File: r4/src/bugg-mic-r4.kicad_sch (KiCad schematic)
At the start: 25 parts, among them J101 2842142-4, U101 PCMD3180

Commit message: Update Wurth spacers to remove DRC violations. DRC pass
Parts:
- H301: renamed from H101; footprint Mounting_Wuerth:Mounting_Wuerth_WA-SMSI-M3_H7mm_9774070360 -> jeffmakes-footprints:Mounting_Wuerth_WA-SMSI-M3_H7mm_9774070360
- H302: renamed from H102; footprint Mounting_Wuerth:Mounting_Wuerth_WA-SMSI-M3_H7mm_9774070360 -> jeffmakes-footprints:Mounting_Wuerth_WA-SMSI-M3_H7mm_9774070360
- renumbered C101 to C301, C102 to C302, C103 to C303, C104 to C304, C105 to C305, C106 to C306, C107 to C307, C108 to C308, C109 to C309, C110 to C310, C111 to C311, C112 to C312, FID1 to FID301, FID2 to FID302, J101 to J301, MIC101 to MIC301, R101 to R301, R102 to R302, R103 to R303, TP102 to TP301, TP103 to TP302, TP101 to TP303, U101 to U301

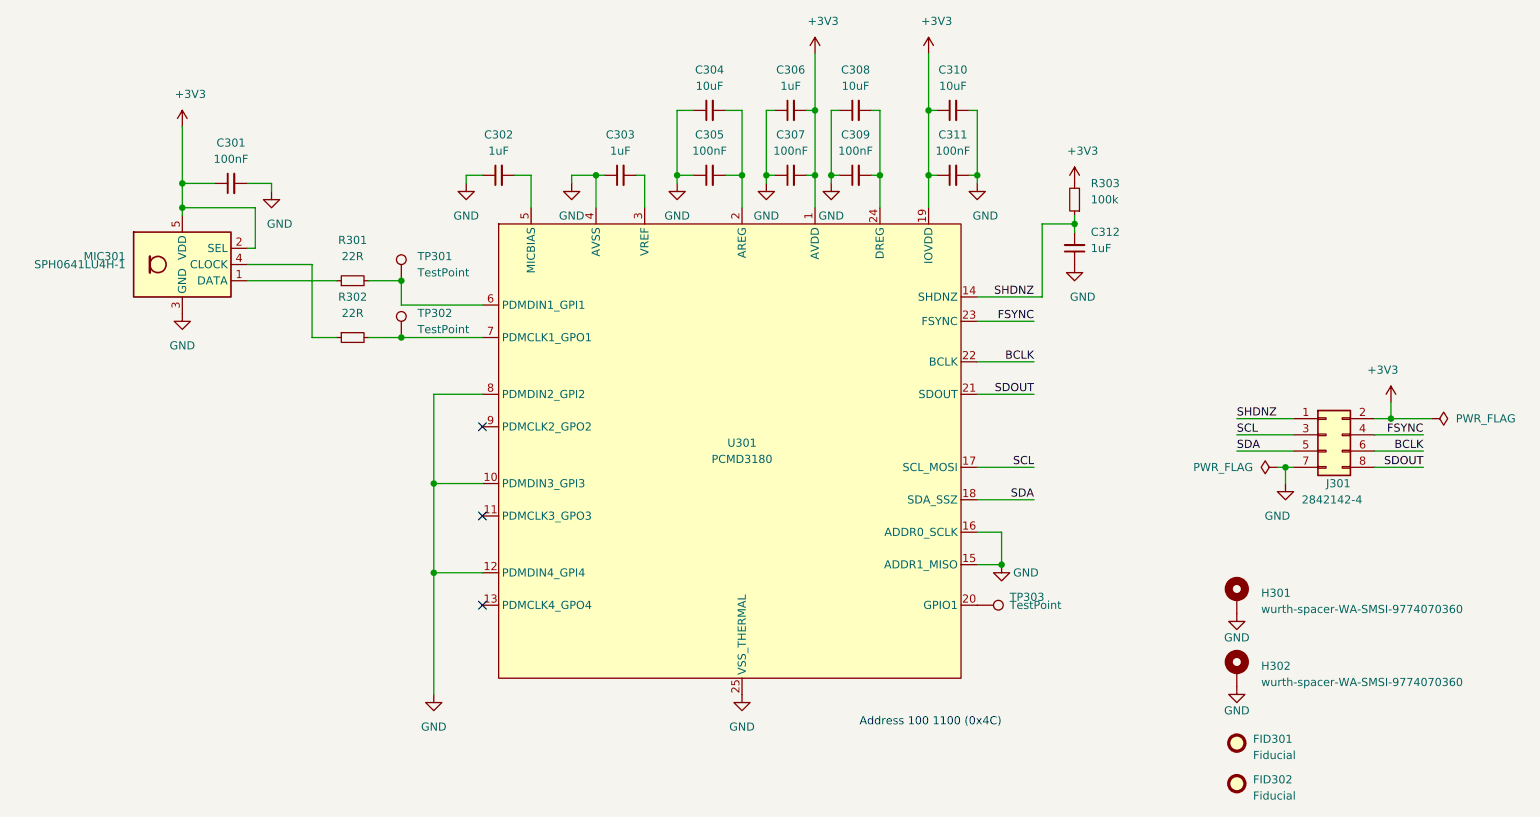
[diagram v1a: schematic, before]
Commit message: Add some cap voltages and other bom-related parameters
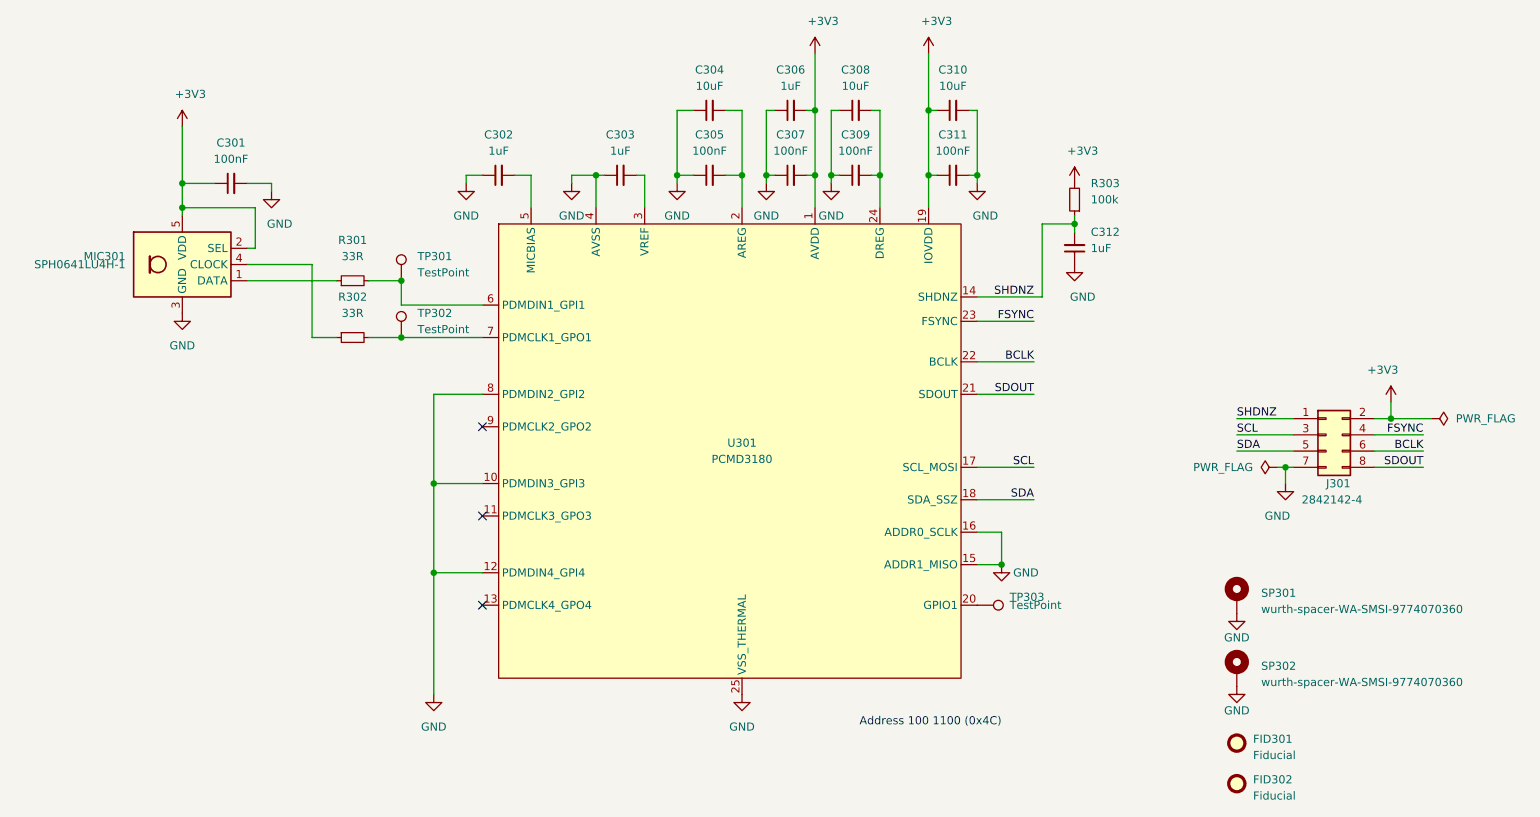
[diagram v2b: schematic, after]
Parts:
- C302, C303, C304, C306, C308, C310: Voltage (none) -> 6.3V
- C312: footprint Capacitor_SMD:C_0603_1608Metric -> Capacitor_SMD:C_0402_1005Metric; Voltage (none) -> 6.3V
- FID301, FID302, TP301, TP302, TP303: now left out of the parts list
- R301, R302: value 22R -> 33R
- renumbered H301 to SP301, H302 to SP302
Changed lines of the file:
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@@
       (effects (font (size 1.27 1.27)))
     )
-    (property "Value" "22R" (at 82.55 80.01 90)
+    (property "Value" "33R" (at 82.55 80.01 90)
       (effects (font (size 1.27 1.27)))
     )
@@
       (project "bugg-mic-r4"
         (path "/1692e6a7-b9c0-4a4a-aa1e-ad946df48101"
-          (reference "R302") (unit 1) (value "22R") (footprint "Resistor_SMD:R_0402_1005Metric")
+          (reference "R302") (unit 1) (value "33R") (footprint "Resistor_SMD:R_0402_1005Metric")
         )
       )
@@
       (effects (font (size 1.27 1.27)) hide)
     )
+    (property "Voltage" "6.3V" (at 105.41 58.42 90)
+      (effects (font (size 1.27 1.27)) hide)
+    )
     (pin "1")
     (pin "2")
@@
   )
   (symbol (lib_id "Connector:TestPoint") (at 90.17 83.82 0) (unit 1)
-    (in_bom yes) (on_board yes) (dnp no)
+    (in_bom no) (on_board yes) (dnp no)
     (property "Reference" "TP302" (at 92.71 80.01 0)
       (effects (font (size 1.27 1.27)) (justify left))
@@
   )
   (symbol (lib_id "Connector:TestPoint") (at 90.17 74.93 0) (unit 1)
-    (in_bom yes) (on_board yes) (dnp no)
+    (in_bom no) (on_board yes) (dnp no)
     (property "Reference" "TP301" (at 92.71 71.12 0)
       (effects (font (size 1.27 1.27)) (justify left))
@@
   (symbol (lib_id "Mechanical:MountingHole_Pad") (at 220.98 135.89 0) (unit 1)
     (in_bom yes) (on_board yes) (dnp no)
-    (property "Reference" "H302" (at 224.79 135.2549 0)
+    (property "Reference" "SP302" (at 224.79 135.2549 0)
       (effects (font (size 1.27 1.27)) (justify left))
     )
@@
       (project "bugg-mic-r4"
         (path "/1692e6a7-b9c0-4a4a-aa1e-ad946df48101"
-          (reference "H302") (unit 1) (value "wurth-spacer-WA-SMSI-9774070360") (footprint "jeffmakes-footprints:Mounting_Wuerth_WA-SMSI-M3_H7mm_9774070360")
+          (reference "SP302") (unit 1) (value "wurth-spacer-WA-SMSI-9774070360") (footprint "jeffmakes-footprints:Mounting_Wuerth_WA-SMSI-M3_H7mm_9774070360")
         )
       )
@@
   )
   (symbol (lib_id "Connector:TestPoint") (at 180.34 125.73 270) (unit 1)
-    (in_bom yes) (on_board yes) (dnp no)
+    (in_bom no) (on_board yes) (dnp no)
     (property "Reference" "TP303" (at 185.42 124.46 90)
       (effects (font (size 1.27 1.27)) (justify left))
@@
       (effects (font (size 1.27 1.27)) hide)
     )
+    (property "Voltage" "6.3V" (at 161.29 48.26 90)
+      (effects (font (size 1.27 1.27)) hide)
+    )
     (pin "1")
     (pin "2")
@@
       (effects (font (size 1.27 1.27)))
     )
-    (property "Value" "22R" (at 82.55 71.12 90)
+    (property "Value" "33R" (at 82.55 71.12 90)
       (effects (font (size 1.27 1.27)))
     )
@@
       (project "bugg-mic-r4"
         (path "/1692e6a7-b9c0-4a4a-aa1e-ad946df48101"
-          (reference "R301") (unit 1) (value "22R") (footprint "Resistor_SMD:R_0402_1005Metric")
+          (reference "R301") (unit 1) (value "33R") (footprint "Resistor_SMD:R_0402_1005Metric")
         )
       )
@@
   )
   (symbol (lib_id "Mechanical:Fiducial") (at 220.98 147.32 0) (unit 1)
-    (in_bom yes) (on_board yes) (dnp no) (fields_autoplaced)
+    (in_bom no) (on_board yes) (dnp no) (fields_autoplaced)
     (property "Reference" "FID301" (at 223.52 146.6849 0)
       (effects (font (size 1.27 1.27)) (justify left))
@@
       (effects (font (size 1.27 1.27)) (justify right))
     )
-    (property "Footprint" "Capacitor_SMD:C_0603_1608Metric" (at 195.58 69.85 0)
+    (property "Footprint" "Capacitor_SMD:C_0402_1005Metric" (at 195.58 69.85 0)
       (effects (font (size 1.27 1.27)) hide)
     )
@@
       (effects (font (size 1.27 1.27)) hide)
     )
-    (pin "1")
-    (pin "2")
-    (instances
-      (project "bugg-mic-r4"
-        (path "/1692e6a7-b9c0-4a4a-aa1e-ad946df48101"
-          (reference "C312") (unit 1) (value "1uF") (footprint "Capacitor_SMD:C_0603_1608Metric")
+    (property "Voltage" "6.3V" (at 195.58 69.85 0)
+      (effects (font (size 1.27 1.27)) hide)
+    )
+    (pin "1")
+    (pin "2")
+    (instances
+      (project "bugg-mic-r4"
+        (path "/1692e6a7-b9c0-4a4a-aa1e-ad946df48101"
+          (reference "C312") (unit 1) (value "1uF") (footprint "Capacitor_SMD:C_0402_1005Metric")
         )
       )
@@
       (effects (font (size 1.27 1.27)) hide)
     )
+    (property "Voltage" "6.3V" (at 151.13 48.26 90)
+      (effects (font (size 1.27 1.27)) hide)
+    )
     (pin "1")
     (pin "2")
@@
       (effects (font (size 1.27 1.27)) hide)
     )
+    (property "Voltage" "6.3V" (at 176.53 48.26 90)
+      (effects (font (size 1.27 1.27)) hide)
+    )
     (pin "1")
     (pin "2")
@@
       (effects (font (size 1.27 1.27)) hide)
     )
+    (property "Voltage" "6.3V" (at 138.43 48.26 90)
+      (effects (font (size 1.27 1.27)) hide)
+    )
     (pin "1")
     (pin "2")
@@
   (symbol (lib_id "Mechanical:MountingHole_Pad") (at 220.98 124.46 0) (unit 1)
     (in_bom yes) (on_board yes) (dnp no)
-    (property "Reference" "H301" (at 224.79 123.8249 0)
+    (property "Reference" "SP301" (at 224.79 123.8249 0)
       (effects (font (size 1.27 1.27)) (justify left))
     )
@@
       (project "bugg-mic-r4"
         (path "/1692e6a7-b9c0-4a4a-aa1e-ad946df48101"
-          (reference "H301") (unit 1) (value "wurth-spacer-WA-SMSI-9774070360") (footprint "jeffmakes-footprints:Mounting_Wuerth_WA-SMSI-M3_H7mm_9774070360")
+          (reference "SP301") (unit 1) (value "wurth-spacer-WA-SMSI-9774070360") (footprint "jeffmakes-footprints:Mounting_Wuerth_WA-SMSI-M3_H7mm_9774070360")
         )
       )
@@
   )
   (symbol (lib_id "Mechanical:Fiducial") (at 220.98 153.67 0) (unit 1)
-    (in_bom yes) (on_board yes) (dnp no) (fields_autoplaced)
+    (in_bom no) (on_board yes) (dnp no) (fields_autoplaced)
     (property "Reference" "FID302" (at 223.52 153.0349 0)
       (effects (font (size 1.27 1.27)) (justify left))
@@
       (effects (font (size 1.27 1.27)) hide)
     )
+    (property "Voltage" "6.3V" (at 124.46 58.42 90)
+      (effects (font (size 1.27 1.27)) hide)
+    )
